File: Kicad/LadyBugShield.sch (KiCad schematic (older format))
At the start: 6 parts, among them P1 CONN_6, P2 CONN_2, P3 BNC, P4 BNC

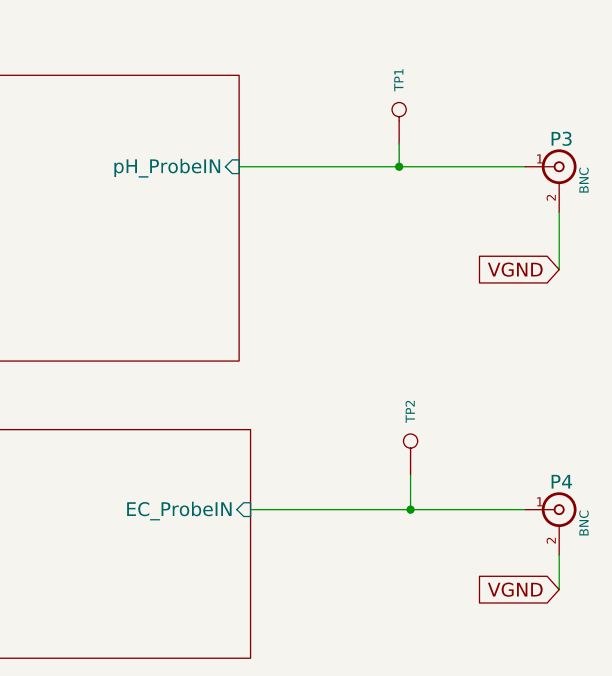
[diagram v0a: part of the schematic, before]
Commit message: fixed BNC connector circuit...still needs final review
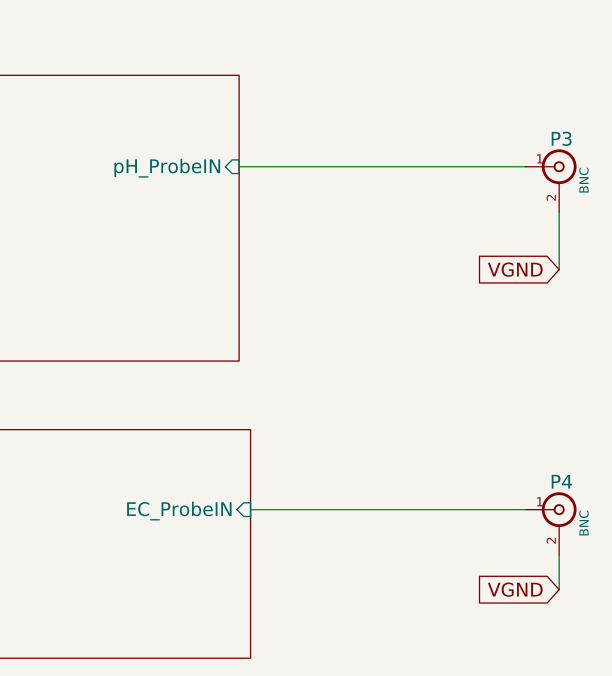
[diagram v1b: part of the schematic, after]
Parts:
- removed TP1, TP2: CONN_1, symbol CONN_1
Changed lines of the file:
@@
 Sheet 1 8
 Title ""
-Date "17 jan 2015"
+Date "21 jan 2015"
 Rev ""
 Comp ""
@@
 Wire Wire Line
 	6050 5800 6550 5800
-$Comp
-L CONN_1 TP1
-U 1 1 54956214
-P 10000 1000
-F 0 "TP1" H 10080 1000 40  0000 L CNN
-F 1 "CONN_1" H 10000 1055 30  0001 C CNN
-F 2 "" H 10000 1000 60  0000 C CNN
-F 3 "" H 10000 1000 60  0000 C CNN
-	1    10000 1000
-	0    -1   -1   0
-$EndComp
-$Comp
-L CONN_1 TP2
-U 1 1 5495627F
-P 10050 2450
-F 0 "TP2" H 10130 2450 40  0000 L CNN
-F 1 "CONN_1" H 10050 2505 30  0001 C CNN
-F 2 "" H 10050 2450 60  0000 C CNN
-F 3 "" H 10050 2450 60  0000 C CNN
-	1    10050 2450
-	0    -1   -1   0
-$EndComp
-Wire Wire Line
-	10000 1150 10000 1250
-Connection ~ 10000 1250
-Wire Wire Line
-	10050 2600 10050 2750
-Connection ~ 10050 2750
 $EndSCHEMATC

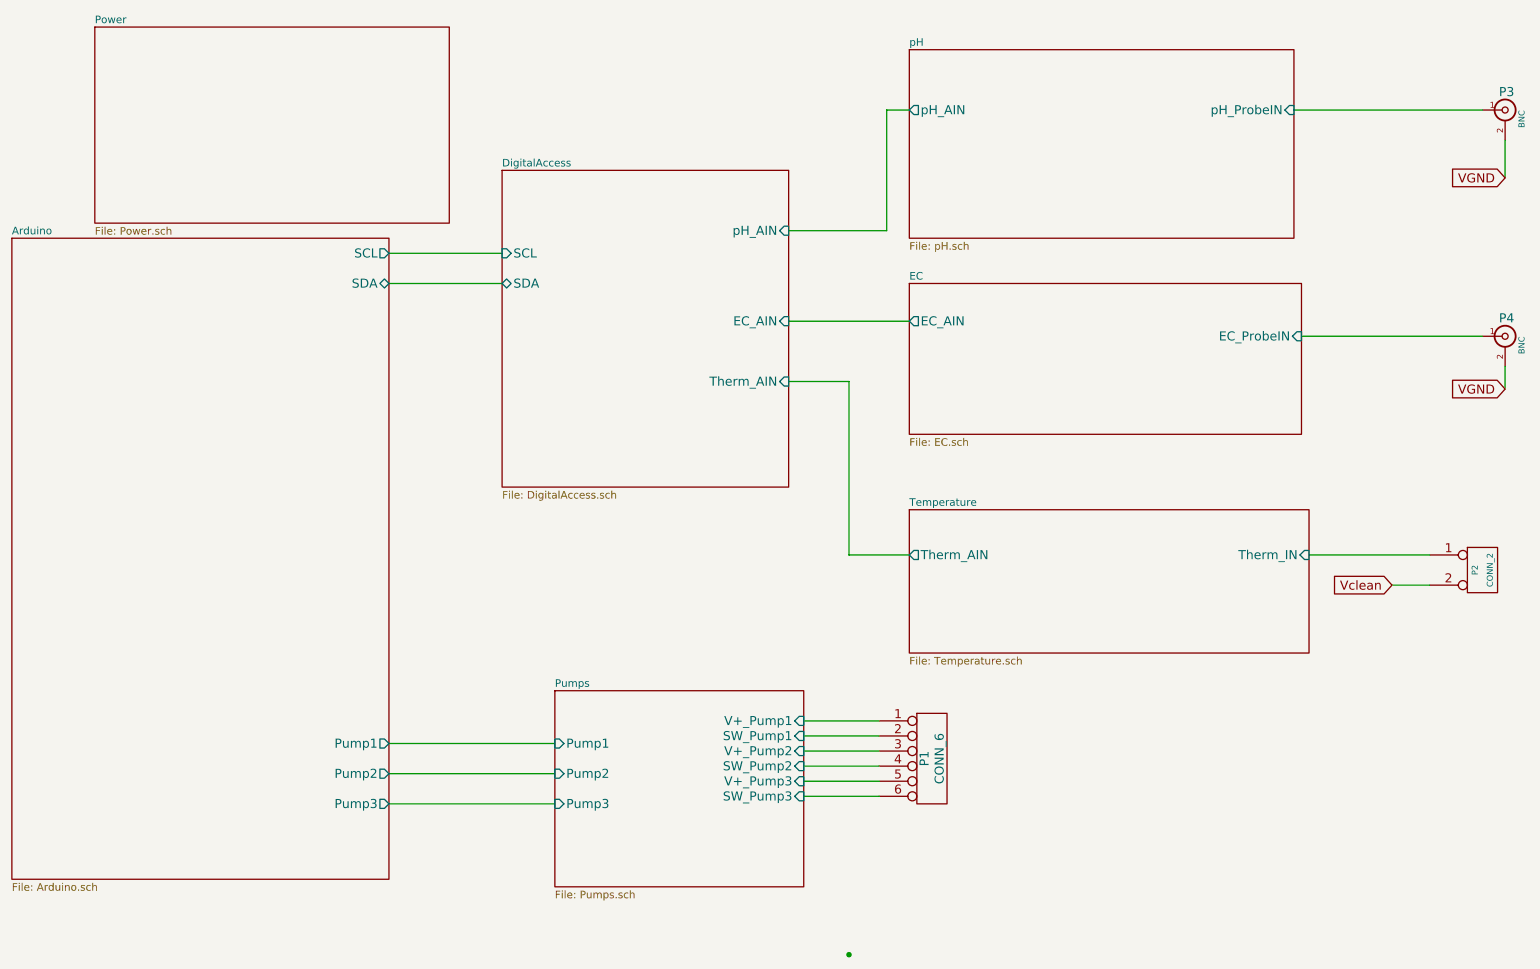
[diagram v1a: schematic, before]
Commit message: added ECTest Arduino Sketch also updates (not all) to the Schematic
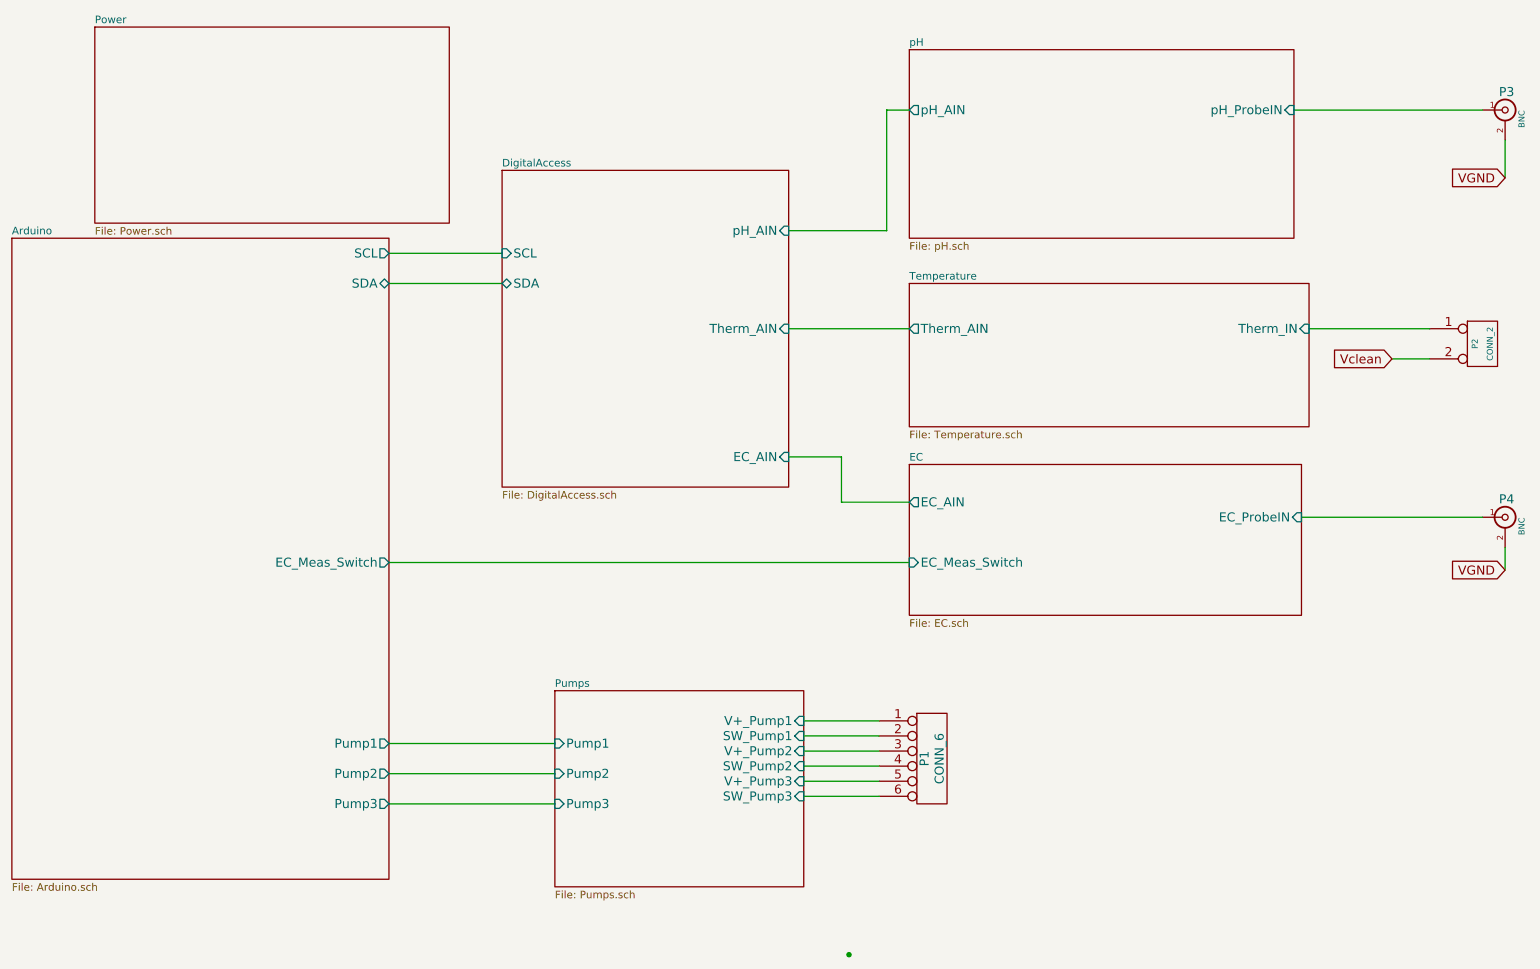
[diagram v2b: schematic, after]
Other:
- moved on the sheet: P2, P4
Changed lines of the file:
@@
 $Descr A4 11693 8268
 encoding utf-8
-Sheet 1 8
+Sheet 1 11
 Title ""
-Date "21 jan 2015"
+Date "29 jan 2015"
 Rev ""
 Comp ""
@@
 F5 "Pump1" O R 3300 5450 60
 F6 "Pump3" O R 3300 5850 60
+F7 "EC_Meas_Switch" O R 3300 4250 60
 $EndSheet
 $Sheet
@@
 F3 "SDA" B L 4050 2400 60
 F4 "pH_AIN" I R 5950 2050 60
-F5 "EC_AIN" I R 5950 2650 60
-F6 "Therm_AIN" I R 5950 3050 60
+F5 "EC_AIN" I R 5950 3550 60
+F6 "Therm_AIN" I R 5950 2700 60
 $EndSheet
 $Sheet
@@
 $EndSheet
 $Sheet
-S 6750 2400 2600 1000
+S 6750 3600 2600 1000
 U 547DE5B0
 F0 "EC" 50
 F1 "EC.sch" 50
-F2 "EC_ProbeIN" I R 9350 2750 60
-F3 "EC_AIN" O L 6750 2650 60
+F2 "EC_ProbeIN" I R 9350 3950 60
+F3 "EC_AIN" O L 6750 3850 60
+F4 "EC_Meas_Switch" I L 6750 4250 60
 $EndSheet
 $Sheet
@@
 	9300 1250 10550 1250
 Wire Wire Line
-	9400 4200 10200 4200
+	9400 2700 10200 2700
 Wire Wire Line
 	6750 1250 6600 1250
@@
 	6600 2050 5950 2050
 Wire Wire Line
-	5950 2650 6750 2650
-Wire Wire Line
 	3300 2200 4050 2200
 Wire Wire Line
@@
 Connection ~ 6350 6850
 $Sheet
-S 6750 3900 2650 950
+S 6750 2400 2650 950
 U 547DE6A0
 F0 "Temperature" 50
 F1 "Temperature.sch" 50
-F2 "Therm_IN" I R 9400 4200 60
-F3 "Therm_AIN" O L 6750 4200 60
+F2 "Therm_IN" I R 9400 2700 60
+F3 "Therm_AIN" O L 6750 2700 60
 $EndSheet
-Wire Wire Line
-	5950 3050 6350 3050
-Wire Wire Line
-	6350 3050 6350 4200
-Wire Wire Line
-	6350 4200 6750 4200
 Text GLabel 10700 1700 0    60   Input ~ 0
 VGND
-Text GLabel 10700 3100 0    60   Input ~ 0
+Text GLabel 10700 4300 0    60   Input ~ 0
 VGND
-Text GLabel 9950 4400 0    60   Input ~ 0
+Text GLabel 9950 2900 0    60   Input ~ 0
 Vclean
 $Comp
@@
 L BNC P4
 U 1 1 54903E31
-P 10700 2750
-F 0 "P4" H 10710 2870 60  0000 C CNN
-F 1 "BNC" V 10810 2690 40  0000 C CNN
-F 2 "~" H 10700 2750 60  0000 C CNN
-F 3 "~" H 10700 2750 60  0000 C CNN
-	1    10700 2750
+P 10700 3950
+F 0 "P4" H 10710 4070 60  0000 C CNN
+F 1 "BNC" V 10810 3890 40  0000 C CNN
+F 2 "~" H 10700 3950 60  0000 C CNN
+F 3 "~" H 10700 3950 60  0000 C CNN
+	1    10700 3950
 	1    0    0    -1
 $EndComp
@@
 L CONN_2 P2
 U 1 1 54903E39
-P 10550 4300
-F 0 "P2" V 10500 4300 40  0000 C CNN
-F 1 "CONN_2" V 10600 4300 40  0000 C CNN
-F 2 "" H 10550 4300 60  0000 C CNN
-F 3 "" H 10550 4300 60  0000 C CNN
-	1    10550 4300
+P 10550 2800
+F 0 "P2" V 10500 2800 40  0000 C CNN
+F 1 "CONN_2" V 10600 2800 40  0000 C CNN
+F 2 "" H 10550 2800 60  0000 C CNN
+F 3 "" H 10550 2800 60  0000 C CNN
+	1    10550 2800
 	1    0    0    -1
 $EndComp
@@
 	10700 1450 10700 1700
 Wire Wire Line
-	10550 2750 9350 2750
+	10550 3950 9350 3950
 Wire Wire Line
-	10700 2950 10700 3100
+	10700 4150 10700 4300
 Wire Wire Line
 	3300 5450 4400 5450
@@
 $EndSheet
 Wire Wire Line
-	9950 4400 10200 4400
+	9950 2900 10200 2900
 Wire Wire Line
 	6550 5300 6050 5300
@@
 Wire Wire Line
 	6050 5800 6550 5800
+Wire Wire Line
+	5950 2700 6750 2700
+Wire Wire Line
+	6750 3850 6300 3850
+Wire Wire Line
+	6300 3850 6300 3550
+Wire Wire Line
+	6300 3550 5950 3550
+Wire Wire Line
+	3300 4250 6750 4250
 $EndSCHEMATC

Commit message: layout for Alpha 2
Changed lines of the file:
@@
 Sheet 1 11
 Title ""
-Date "29 jan 2015"
+Date "8 feb 2015"
 Rev ""
 Comp ""
@@
 F5 "Pump1" O R 3300 5450 60
 F6 "Pump3" O R 3300 5850 60
-F7 "EC_Meas_Switch" O R 3300 4250 60
+F7 "MUX_out_pin" O R 3300 4250 60
+F8 "FET_pin" O R 3300 4450 60
+F9 "MUX_enable_pin" O R 3300 4050 60
 $EndSheet
 $Sheet
@@
 F2 "EC_ProbeIN" I R 9350 3950 60
 F3 "EC_AIN" O L 6750 3850 60
-F4 "EC_Meas_Switch" I L 6750 4250 60
+F4 "MUX_out_pin" I L 6750 4250 60
+F5 "FET_pin" I L 6750 4450 60
+F6 "MUX_enable_pin" I L 6750 4050 60
 $EndSheet
 $Sheet
@@
 	6300 3550 5950 3550
 Wire Wire Line
+	3300 4050 6750 4050
+Wire Wire Line
 	3300 4250 6750 4250
+Wire Wire Line
+	3300 4450 6750 4450
 $EndSCHEMATC
